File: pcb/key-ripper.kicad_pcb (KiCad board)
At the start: 2 copper layers, 290.5 x 123.8 mm, 193 parts, among them J1 Conn_01x04, SW1 ESC, SW10 F9, SW11 F10, SW12 F11, SW13 F12, SW14 TILDE, SW15 1, SW16 2, SW17 3, SW18 4, SW19 5, SW2 F1, SW20 6, SW21 7, SW22 8, SW23 9, SW24 0, SW25 -, SW26 +, SW27 BACKSPACE, SW28 TAB, SW29 Q, SW3 F2, SW30 W, SW31 E, SW32 R, SW33 T, SW34 Y, SW35 U, SW36 I, SW37 O, SW38 P, SW39 [, SW4 F3, SW40 ], SW41 BACKSLASH, SW42 CAPS, SW43 A, SW44 S, SW45 D, SW46 F, SW47 G, SW48 H, SW49 J, SW5 F4, SW50 K, SW51 L, SW52 ;, SW53 ', SW54 ENTER, SW55 L_SHIFT, SW56 Z, SW57 X, SW58 C, SW59 V, SW6 F5, SW60 B, SW61 N, SW62 M, SW63 ,, SW64 ., SW65 FWD_SLASH, SW66 UP, SW67 FN, SW68 BL_CTRL, SW69 L_ALT, SW7 F6, SW70 L_CMD, SW71 SPACE, SW72 R_CMD, SW73 LEFT, SW74 DOWN, SW75 RIGHT, SW8 F7, SW9 F8, U1 RP2040, U2 TYPE-C-31-M-12, U3 XC6206PxxxMR, U4 W25Q128JVS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

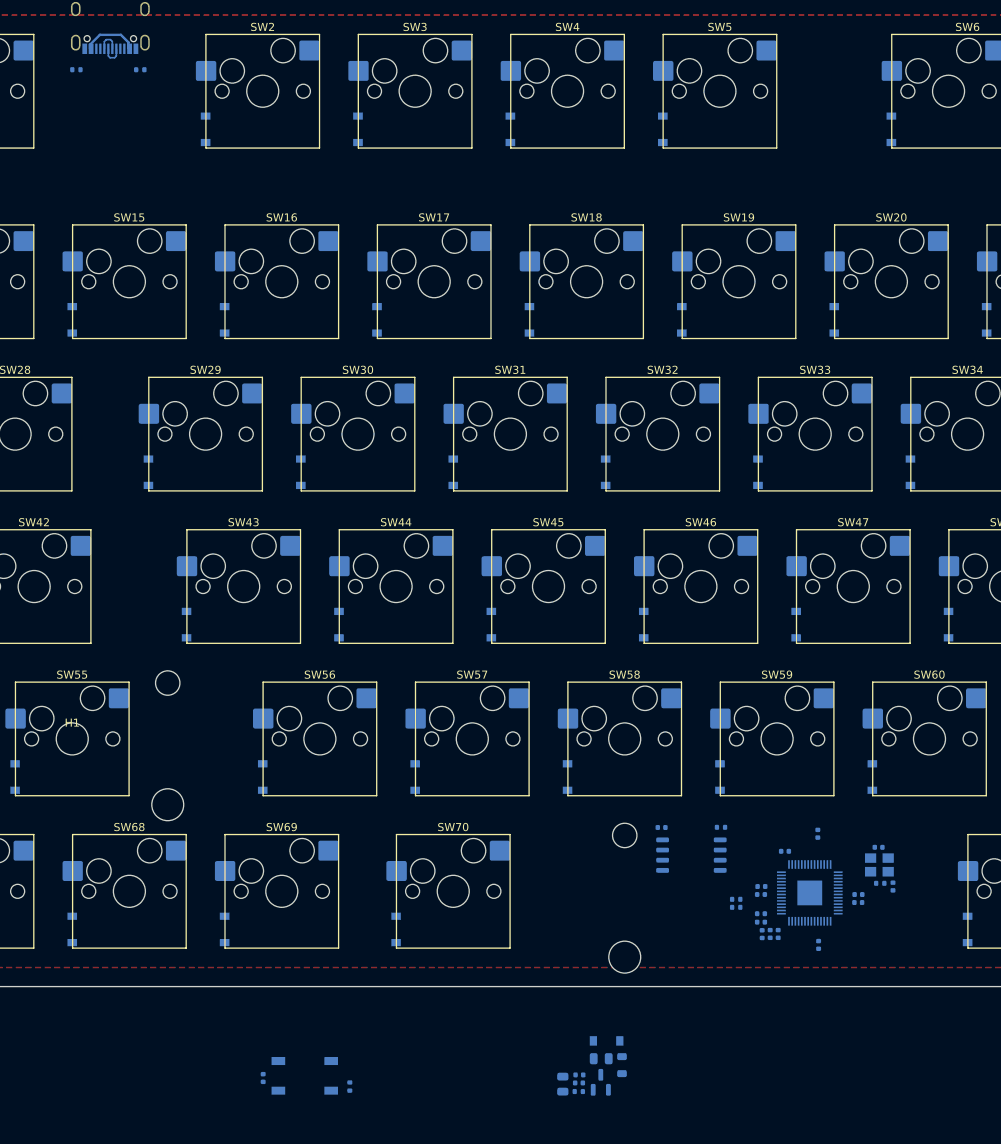
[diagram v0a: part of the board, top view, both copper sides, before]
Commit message: Update PCB with new matrix layout
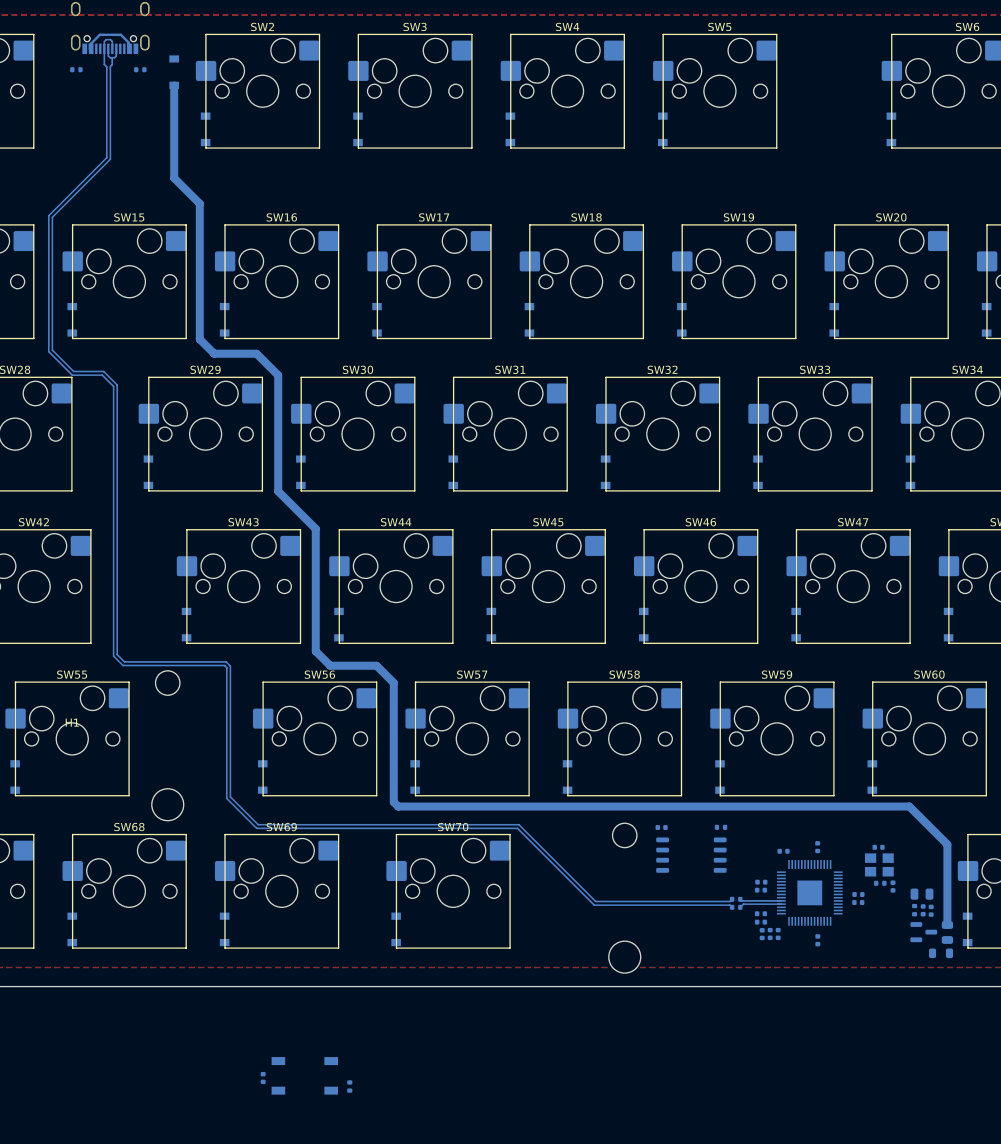
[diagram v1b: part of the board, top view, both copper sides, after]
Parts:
- moved D76 132.6 mm to (24.6, -26.2), turned to 90 degrees
- moved D77 50.8 mm to (118.1, 76.5), turned to 180 degrees
- moved C4 48.5 mm to (119.3, 78.6), turned to 90 degrees
- moved C5 48.1 mm to (118.3, 78.6), turned to 90 degrees
- moved R9 47.7 mm to (117.2, 78.5), turned to 90 degrees
- moved F1 46.1 mm to (121.3, 81.3), turned to -90 degrees
- moved U3 44.5 mm to (118.3, 81.3), turned to 0 degrees
- moved FB1 42.3 mm to (120.5, 84.0), turned to 180 degrees
- moved C12 1.68 mm to (105.1, 70.7)
- moved C10 0.59 mm to (105.1, 82.3)
- moved C14 0.55 mm to (98.0, 76.0)
- moved C16 0.55 mm to (98.0, 75.0)
- moved C13 0.18 mm to (100.8, 71.2)
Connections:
- SW10 pad 2: CLM9 -> CLM10
- SW11 pad 2: CLM10 -> CLM11
- SW12 pad 2: CLM11 -> CLM12
- SW13 pad 2: CLM12 -> CLM13
- SW56 pad 2: CLM1 -> CLM2
- SW57 pad 2: CLM2 -> CLM3
- SW58 pad 2: CLM3 -> CLM4
- SW59 pad 2: CLM4 -> CLM5
- SW60 pad 2: CLM5 -> CLM6
- SW61 pad 2: CLM6 -> CLM7
- SW62 pad 2: CLM7 -> CLM8
- SW63 pad 2: CLM8 -> CLM9
- SW64 pad 2: CLM9 -> CLM10
- SW65 pad 2: CLM10 -> CLM11
- SW66 pad 2: CLM11 -> CLM12
- SW7 pad 2: CLM6 -> CLM7
- SW71 pad 2: CLM4 -> CLM6
- SW72 pad 2: CLM5 -> CLM10
- SW73 pad 2: CLM6 -> CLM11
- SW74 pad 2: CLM7 -> CLM12
- SW75 pad 2: CLM8 -> CLM13
- SW8 pad 2: CLM7 -> CLM8
- SW9 pad 2: CLM8 -> CLM9
- U1 pad 11: CLM8 -> unconnected-(U1-Pad11)
- U1 pad 12: CLM9 -> unconnected-(U1-Pad12)
- U1 pad 13: CLM10 -> unconnected-(U1-Pad13)
- U1 pad 14: CLM11 -> unconnected-(U1-Pad14)
- U1 pad 15: CLM12 -> unconnected-(U1-Pad15)
- U1 pad 16: CLM13 -> unconnected-(U1-Pad16)
- U1 pad 17: ROW0 -> unconnected-(U1-Pad17)
- U1 pad 18: ROW1 -> unconnected-(U1-Pad18)
- U1 pad 2: CLM0 -> ROW0
- U1 pad 27: ROW2 -> CLM13
- U1 pad 28: ROW3 -> CLM12
- U1 pad 29: ROW4 -> CLM11
- U1 pad 3: CLM1 -> ROW1
- U1 pad 30: ROW5 -> CLM10
- U1 pad 31: unconnected-(U1-Pad31) -> CLM9
- U1 pad 32: unconnected-(U1-Pad32) -> CLM8
- U1 pad 34: unconnected-(U1-Pad34) -> CLM7
- U1 pad 35: unconnected-(U1-Pad35) -> CLM6
- U1 pad 36: unconnected-(U1-Pad36) -> CLM5
- U1 pad 37: unconnected-(U1-Pad37) -> CLM4
- U1 pad 38: unconnected-(U1-Pad38) -> CLM3
- U1 pad 39: unconnected-(U1-Pad39) -> CLM2
- U1 pad 4: CLM2 -> ROW2
- U1 pad 40: unconnected-(U1-Pad40) -> CLM1
- U1 pad 41: unconnected-(U1-Pad41) -> CLM0
- U1 pad 5: CLM3 -> ROW3
- U1 pad 6: CLM4 -> ROW4
- U1 pad 7: CLM5 -> ROW5
- U1 pad 8: CLM6 -> unconnected-(U1-Pad8)
- U1 pad 9: CLM7 -> unconnected-(U1-Pad9)
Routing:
- net Net-(D76-Pad1): track 0.00 -> 188.9 mm
- net USB-: track 3.01 -> 187.5 mm
- net USB+: track 2.98 -> 185.6 mm
- net USB_MCU-: track 0.00 -> 5.31 mm
- net USB_MCU+: track 0.00 -> 5.22 mm

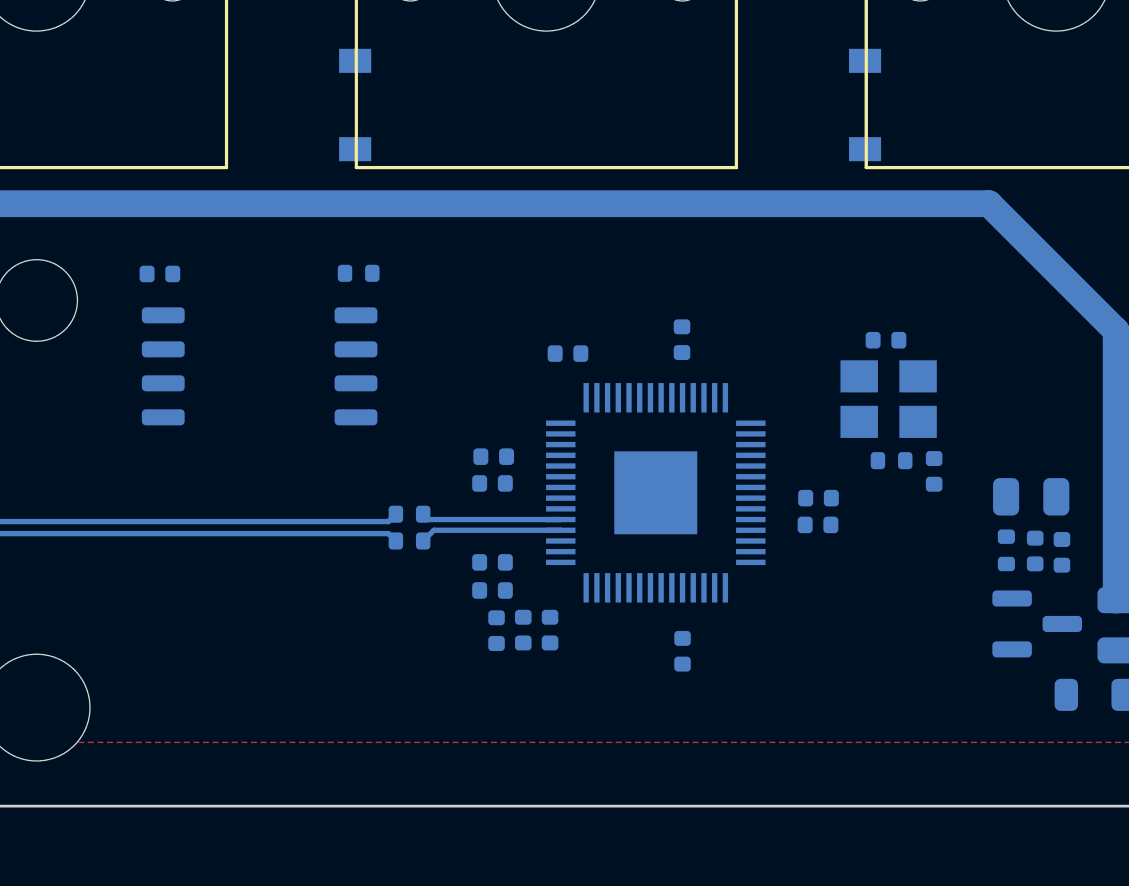
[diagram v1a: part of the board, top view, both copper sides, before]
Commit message: Organize key matrix vias
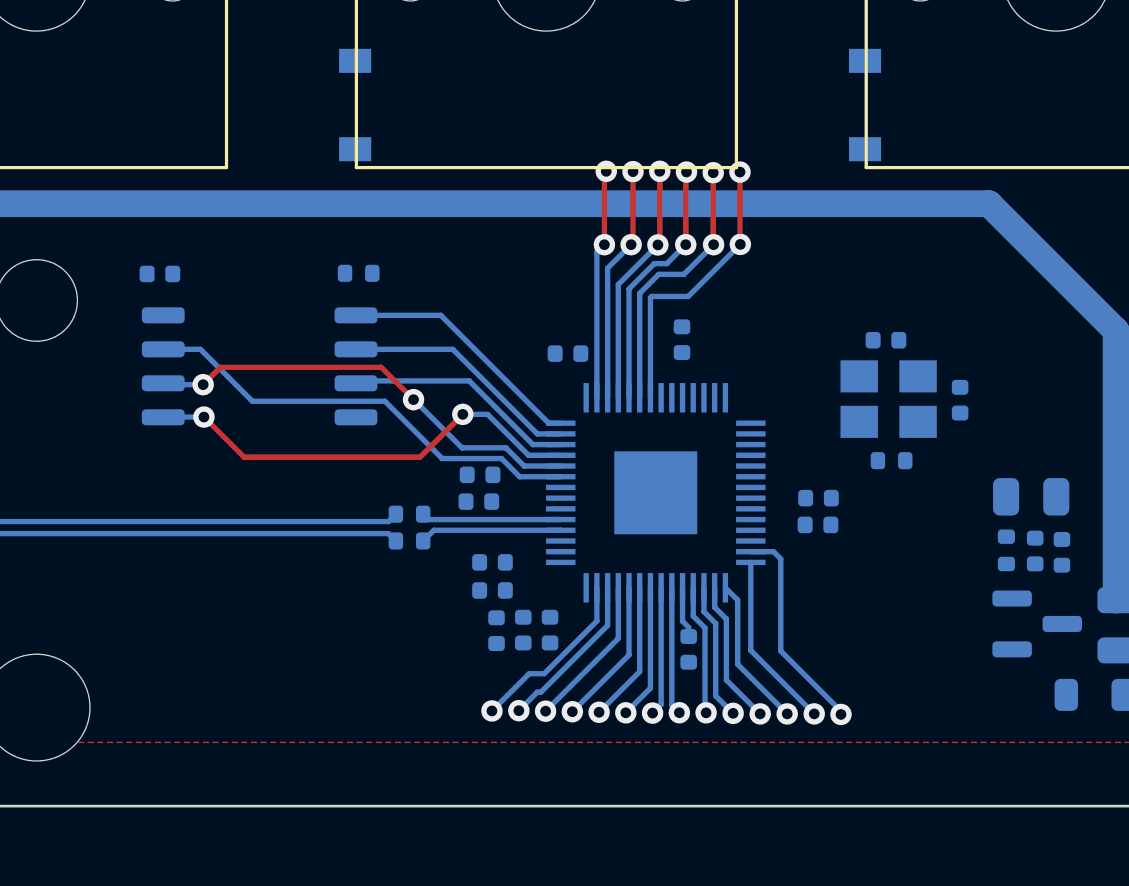
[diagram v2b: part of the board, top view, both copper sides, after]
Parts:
- moved C7 2.83 mm to (115.5, 72.9), turned to 90 degrees
- moved C14 0.85 mm to (97.5, 76.7)
- moved C16 0.85 mm to (97.5, 75.7)
- moved C10 0.24 mm to (105.3, 82.2)
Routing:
- net QSPI_SD3: track 0.00 -> 16.8 mm
- net QSPI_SD0: track 0.00 -> 16.8 mm, vias 0 -> 2
- net QSPI_SCLK: track 0.00 -> 16.7 mm, vias 0 -> 2
- net ROW5: track 0.00 -> 10.6 mm, vias 0 -> 2
- net ROW4: track 0.00 -> 10.1 mm, vias 0 -> 2
- net ROW3: track 0.00 -> 9.60 mm, vias 0 -> 2
- net QSPI_SS: track 0.00 -> 9.32 mm
- net ROW2: track 0.00 -> 9.10 mm, vias 0 -> 2
- net QSPI_SD1: track 0.00 -> 8.96 mm
- net ROW1: track 0.00 -> 8.84 mm, vias 0 -> 2
- net QSPI_SD2: track 0.00 -> 8.67 mm
- net ROW0: track 0.00 -> 8.60 mm, vias 0 -> 2
- net CLM13: track 0.00 -> 7.97 mm, vias 0 -> 1
- net CLM12: track 0.00 -> 6.64 mm, vias 0 -> 1
- net CLM0: track 0.00 -> 6.55 mm, vias 0 -> 1
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
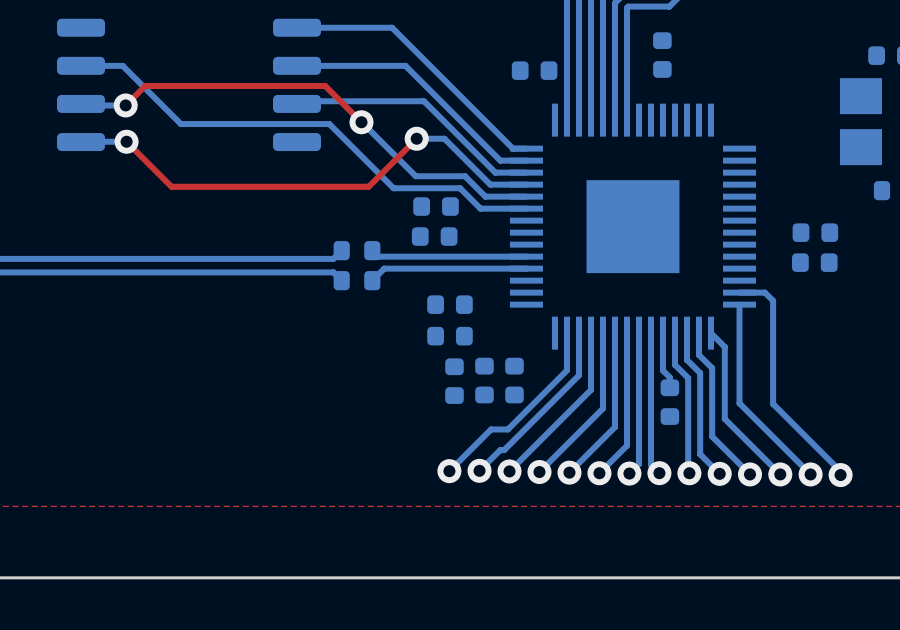
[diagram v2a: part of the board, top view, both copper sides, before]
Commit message: Move some silkscreens
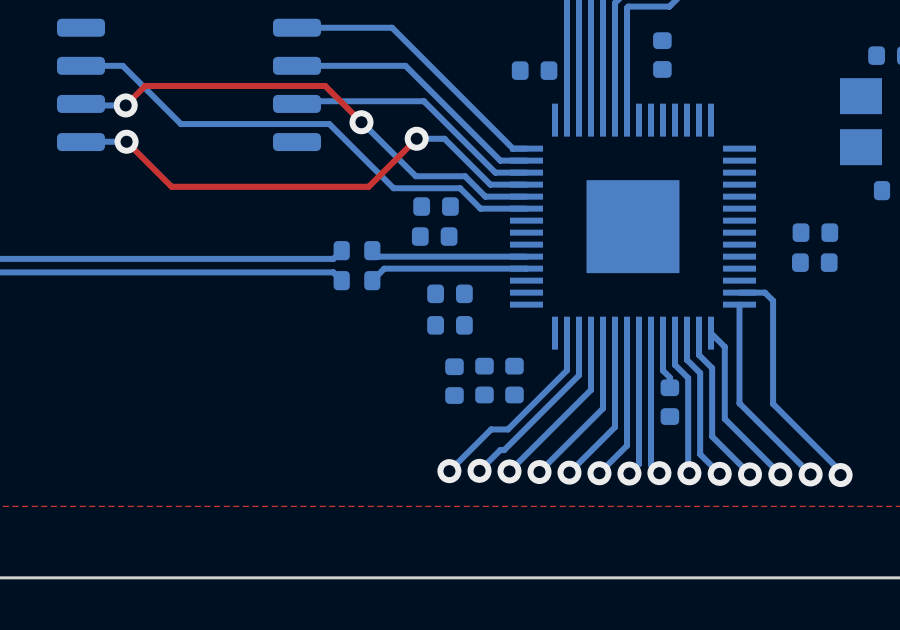
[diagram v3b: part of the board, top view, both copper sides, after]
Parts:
- moved C2 0.36 mm to (98.0, 78.6)
- moved C8 0.36 mm to (98.0, 79.7)
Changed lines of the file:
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@@
     (property "Sheetname" "")
     (attr smd)
-    (fp_text reference "C9" (at 1.97 -0.05 -270) (layer "B.SilkS")
+    (fp_text reference "C9" (at 1.97 3.8 -270) (layer "B.SilkS")
       (effects (font (size 1 1) (thickness 0.15)) (justify mirror))
     )
@@
   )
   (footprint "Capacitor_SMD:C_0402_1005Metric" (layer "B.Cu")
-    (at 98 79 180)
+    (at 98 78.64 180)
     (descr "Capacitor SMD 0402 (1005 Metric), square (rectangular) end terminal, IPC_7351 nominal, (Body size source: IPC-SM-782 page 76, https://www.pcb-3d.com/wordpress/wp-content/uploads/ipc-sm-782a_amendment_1_and_2.pdf), generated with kicad-footprint-generator")
     (tags "capacitor")
@@
     (property "Sheetname" "")
     (attr smd)
-    (fp_text reference "C2" (at 2 -0.4) (layer "B.SilkS")
+    (fp_text reference "C2" (at 1.91 -0.78) (layer "B.SilkS")
       (effects (font (size 1 1) (thickness 0.15)) (justify mirror))
     )
@@
     (property "Sheetname" "")
     (attr smd)
-    (fp_text reference "C1" (at 1.95 0.55 -270) (layer "B.SilkS")
+    (fp_text reference "C1" (at 1.95 4.4 -270) (layer "B.SilkS")
       (effects (font (size 1 1) (thickness 0.15)) (justify mirror))
     )
@@
   )
   (footprint "Capacitor_SMD:C_0402_1005Metric" (layer "B.Cu")
-    (at 98 80.05 180)
+    (at 98 79.69 180)
     (descr "Capacitor SMD 0402 (1005 Metric), square (rectangular) end terminal, IPC_7351 nominal, (Body size source: IPC-SM-782 page 76, https://www.pcb-3d.com/wordpress/wp-content/uploads/ipc-sm-782a_amendment_1_and_2.pdf), generated with kicad-footprint-generator")
     (tags "capacitor")
@@
     (property "Sheetname" "")
     (attr smd)
-    (fp_text reference "C8" (at 2 -0.75) (layer "B.SilkS")
+    (fp_text reference "C8" (at 1.91 -1.13) (layer "B.SilkS")
       (effects (font (size 1 1) (thickness 0.15)) (justify mirror))
     )
@@
     (property "Sheetname" "")
     (attr smd)
-    (fp_text reference "C15" (at 2.37 -0.55 -270) (layer "B.SilkS")
+    (fp_text reference "C15" (at 2.37 3.3 -270) (layer "B.SilkS")
       (effects (font (size 1 1) (thickness 0.15)) (justify mirror))
     )

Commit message: Move Fn row down to be flush with number row
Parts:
- moved D1 4.76 mm to (-7.14, -14.3)
- moved D10 4.76 mm to (202.4, -14.3)
- moved D11 4.76 mm to (221.5, -14.3)
- moved D12 4.76 mm to (240.5, -14.3)
- moved D13 4.76 mm to (259.6, -14.3)
- moved D2 4.76 mm to (28.6, -14.3)
- moved D3 4.76 mm to (47.6, -14.3)
- moved D4 4.76 mm to (66.7, -14.3)
- moved D5 4.76 mm to (85.7, -14.3)
- moved D6 4.76 mm to (114.3, -14.3)
- moved D7 4.76 mm to (135.7, -14.3)
- moved D8 4.76 mm to (154.8, -14.3)
- moved D9 4.76 mm to (173.8, -14.3)
- moved SW1 4.76 mm to (0.00, -19.1)
- moved SW10 4.76 mm to (209.6, -19.1)
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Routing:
- net USB-: track 187.5 -> 173.8 mm
- net USB+: track 185.6 -> 172.8 mm
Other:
- board size 290.5 x 123.8 mm -> 290.5 x 121.4 mm
